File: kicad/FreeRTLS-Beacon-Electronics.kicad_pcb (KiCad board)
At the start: 2 copper layers, 52.5 x 33.5 mm, 0 parts

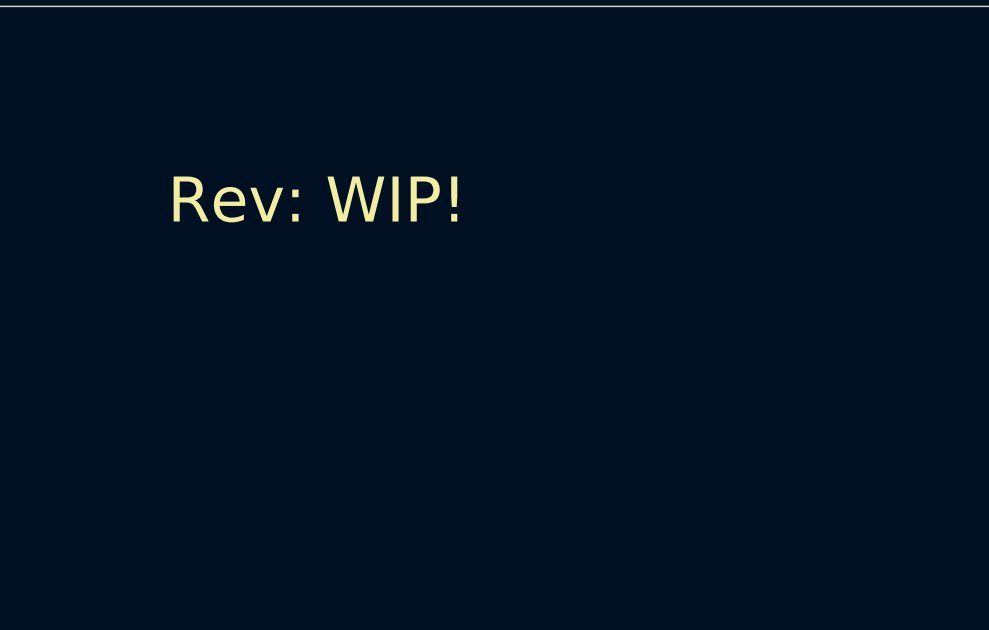
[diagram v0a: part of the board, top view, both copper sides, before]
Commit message: Add trace to test cnc file generation
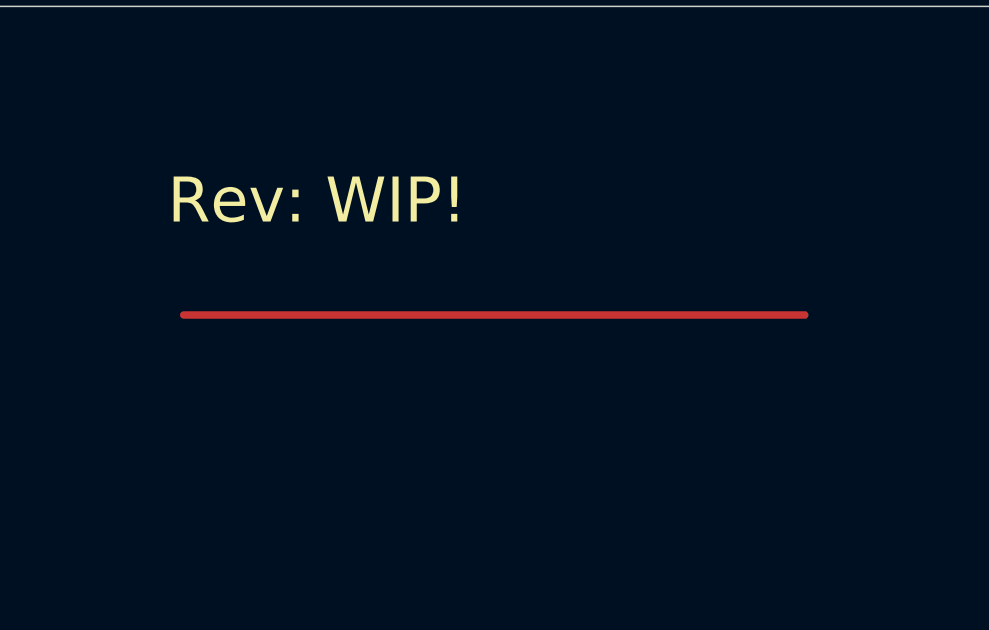
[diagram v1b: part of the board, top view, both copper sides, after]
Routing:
- net (no net): track 0.00 -> 20.7 mm
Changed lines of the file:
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@@
     (thickness 1.6)
     (drawings 5)
-    (tracks 0)
+    (tracks 1)
     (zones 0)
     (modules 0)
@@
     (effects (font (size 1.5 1.5) (thickness 0.3)))
   )
+  (segment (start 93.218 70.866) (end 113.919 70.866) (width 0.25) (layer F.Cu) (net 0))
 )

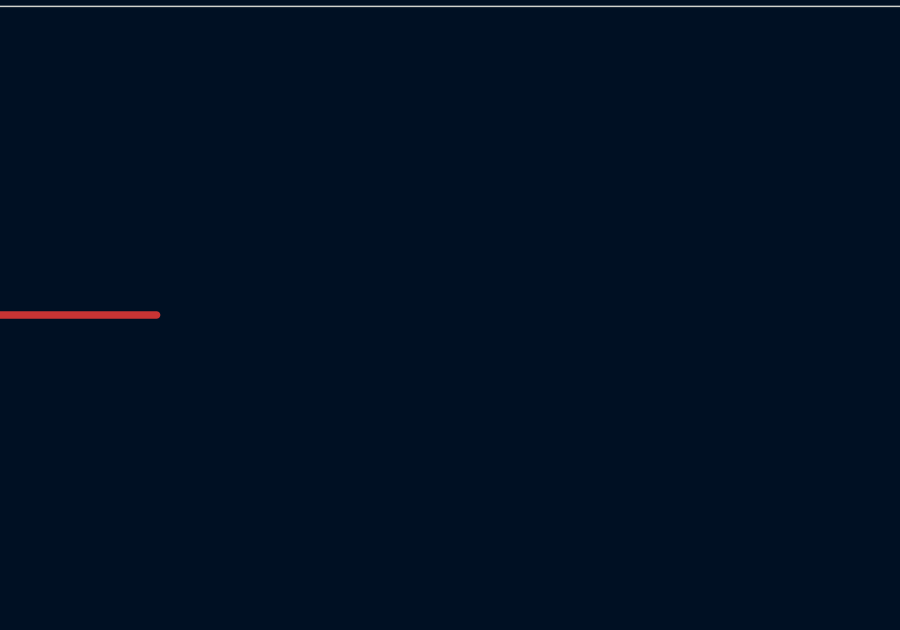
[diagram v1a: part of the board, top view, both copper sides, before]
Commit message: Add via to test cnc file generation
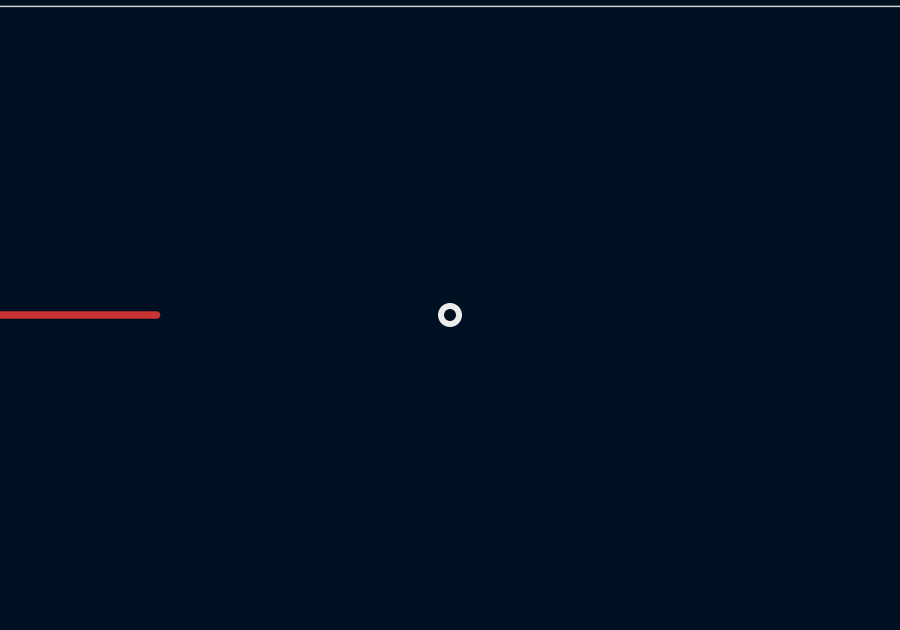
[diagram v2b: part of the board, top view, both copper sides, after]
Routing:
- net (no net): vias 0 -> 1
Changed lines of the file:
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@@
     (thickness 1.6)
     (drawings 5)
-    (tracks 1)
+    (tracks 2)
     (zones 0)
     (modules 0)
@@
   )
   (segment (start 93.218 70.866) (end 113.919 70.866) (width 0.25) (layer F.Cu) (net 0))
+  (via (at 123.698 70.866) (size 0.8) (drill 0.4) (layers F.Cu B.Cu) (net 0))
 )

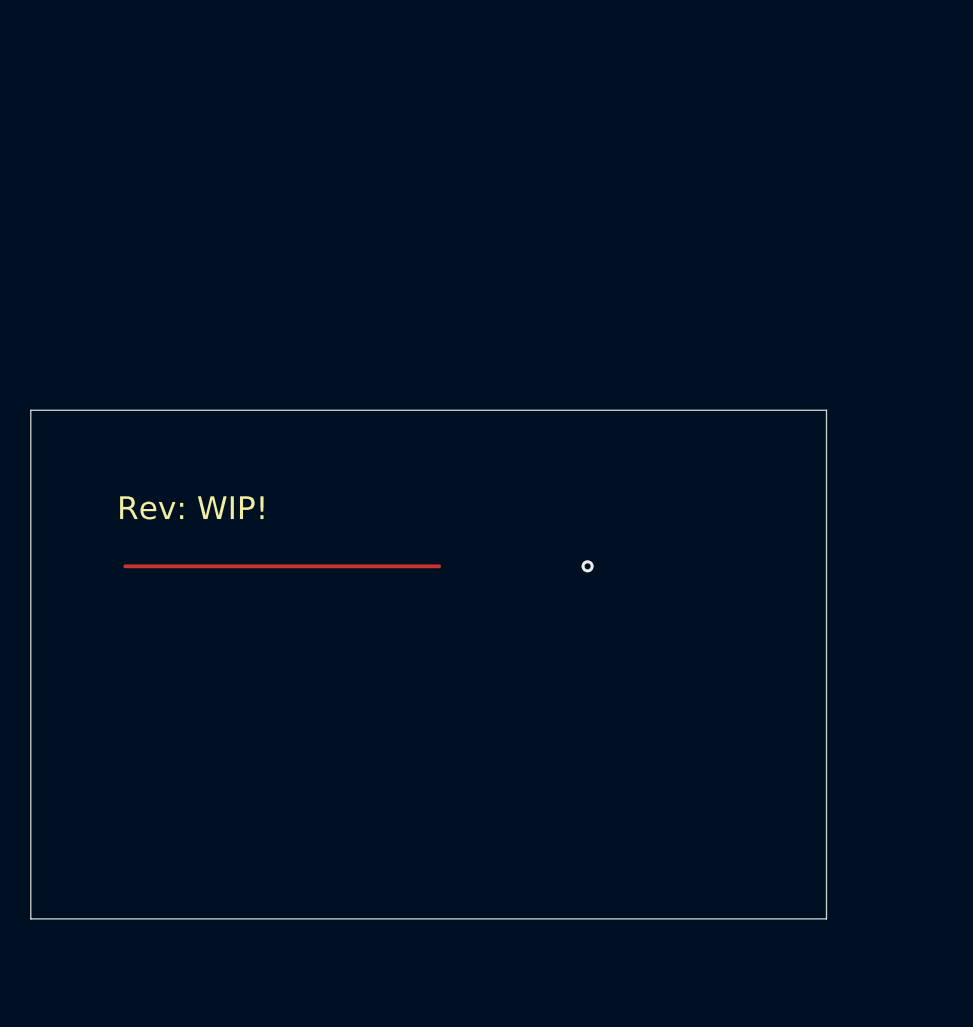
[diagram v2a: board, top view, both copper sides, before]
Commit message: Assign footprints
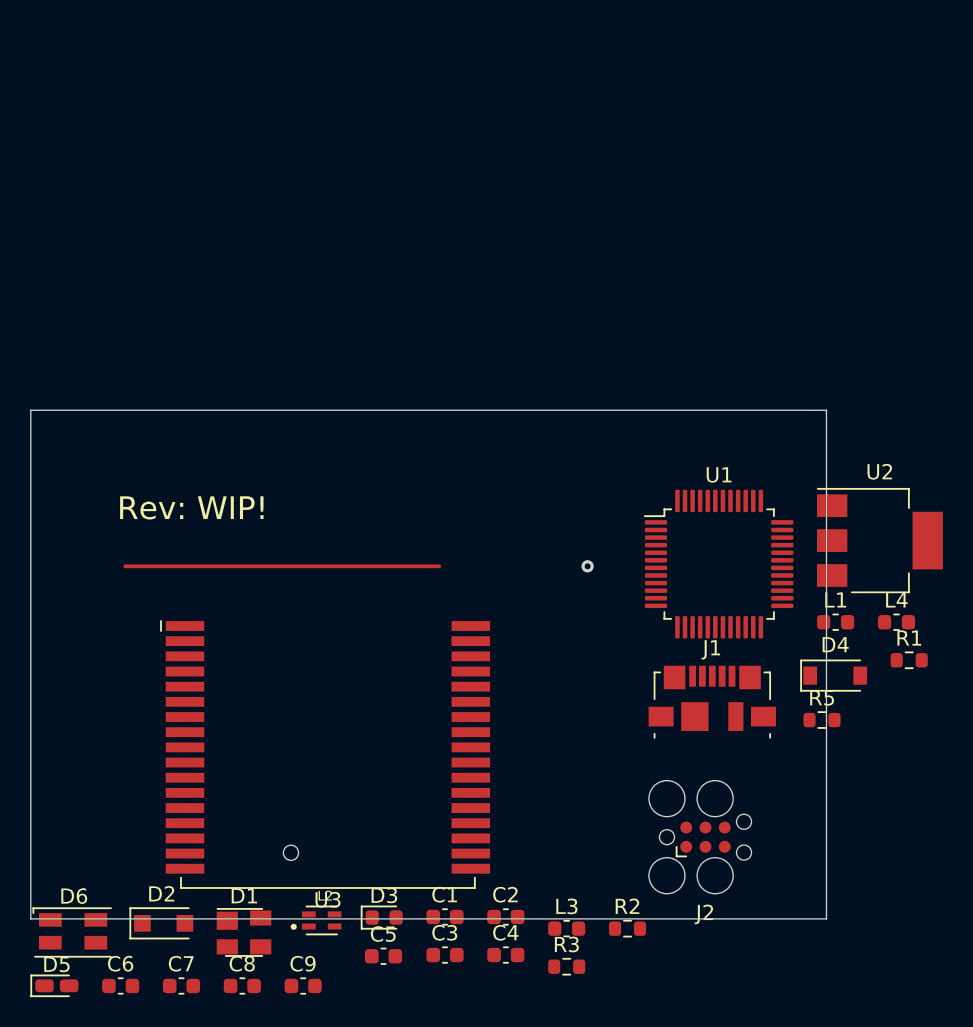
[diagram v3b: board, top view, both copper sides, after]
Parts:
- added C1: 1uF, Capacitor_SMD:C_0603_1608Metric, F.Cu at (114.3, 94.0)
- added C2: 100nF, Capacitor_SMD:C_0603_1608Metric, F.Cu at (118.3, 94.0)
- added C3: 100nF, Capacitor_SMD:C_0603_1608Metric, F.Cu at (114.3, 96.5)
- added C4: 100nF, Capacitor_SMD:C_0603_1608Metric, F.Cu at (118.3, 96.5)
- added C5: 100nF, Capacitor_SMD:C_0603_1608Metric, F.Cu at (110.2, 96.6)
- added C6: 10uF, Capacitor_SMD:C_0603_1608Metric, F.Cu at (92.9, 98.5)
- added C7: 10uF, Capacitor_SMD:C_0603_1608Metric, F.Cu at (96.9, 98.5)
- added C8: 10uF, Capacitor_SMD:C_0603_1608Metric, F.Cu at (100.9, 98.5)
- added C9: 100nF, Capacitor_SMD:C_0603_1608Metric, F.Cu at (105.0, 98.5)
- added D1: PRTR5V0U2X, Package_TO_SOT_SMD:SOT-143, F.Cu at (101.0, 95.0)
- added D2: PMEG3020EH, Diode_SMD:D_SOD-123F, F.Cu at (95.8, 94.4)
- added D3: LED GREEN, LED_SMD:LED_0603_1608Metric, F.Cu at (110.3, 94.0)
- added D4: 5.6V 1W, Diode_SMD:D_SOD-123, F.Cu at (140.0, 78.1)
- added D5: LED RED, LED_SMD:LED_0603_1608Metric_Castellated, F.Cu at (88.7, 98.5)
- added D6: L955QEQGC-TR, FreeRTLS-Beacon:LED_L955QEQGC-TR_3.2x2.7mm_P1.7mm, F.Cu at (89.8, 94.9)
- added J1: USB_B_Micro, Connector_USB:USB_Micro-B_Molex_47346-0001, F.Cu at (131.9, 79.6)
- added J2: TC2030, Connector:Tag-Connect_TC2030-IDC-FP_2x03_P1.27mm_Vertical, F.Cu at (131.5, 88.7)
- added L1: MPZ1608S221ATA00, Inductor_SMD:L_0603_1608Metric, F.Cu at (140.1, 74.5)
- added L2: DLW21HN900SQ2, FreeRTLS-Beacon:FIL_DLW21HN900SQ2L, F.Cu at (106.2, 94.2)
- added L3: MPZ1608S601ATA00, Inductor_SMD:L_0603_1608Metric, F.Cu at (122.3, 94.8)
- added L4: MPZ1608S221ATA00, Inductor_SMD:L_0603_1608Metric, F.Cu at (144.1, 74.5)
- added R1: 1k, Resistor_SMD:R_0603_1608Metric, F.Cu at (144.9, 77.1)
- added R2: 1k, Resistor_SMD:R_0603_1608Metric, F.Cu at (126.3, 94.8)
- added R3: 1k, Resistor_SMD:R_0603_1608Metric, F.Cu at (122.3, 97.3)
- added R5: 470, Resistor_SMD:R_0603_1608Metric, F.Cu at (139.2, 81.0)
- added U1: STM32F072CBTx, Package_QFP:LQFP-48_7x7mm_P0.5mm, F.Cu at (132.4, 70.7)
- added U2: AZ1117IH-3.3TRG1, Package_TO_SOT_SMD:SOT-223-3_TabPin2, F.Cu at (143.0, 69.2)
- added U3: DWM1001, RF_Module:DecaWave_DWM1001, F.Cu at (106.6, 82.9)

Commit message: Place all components and route some
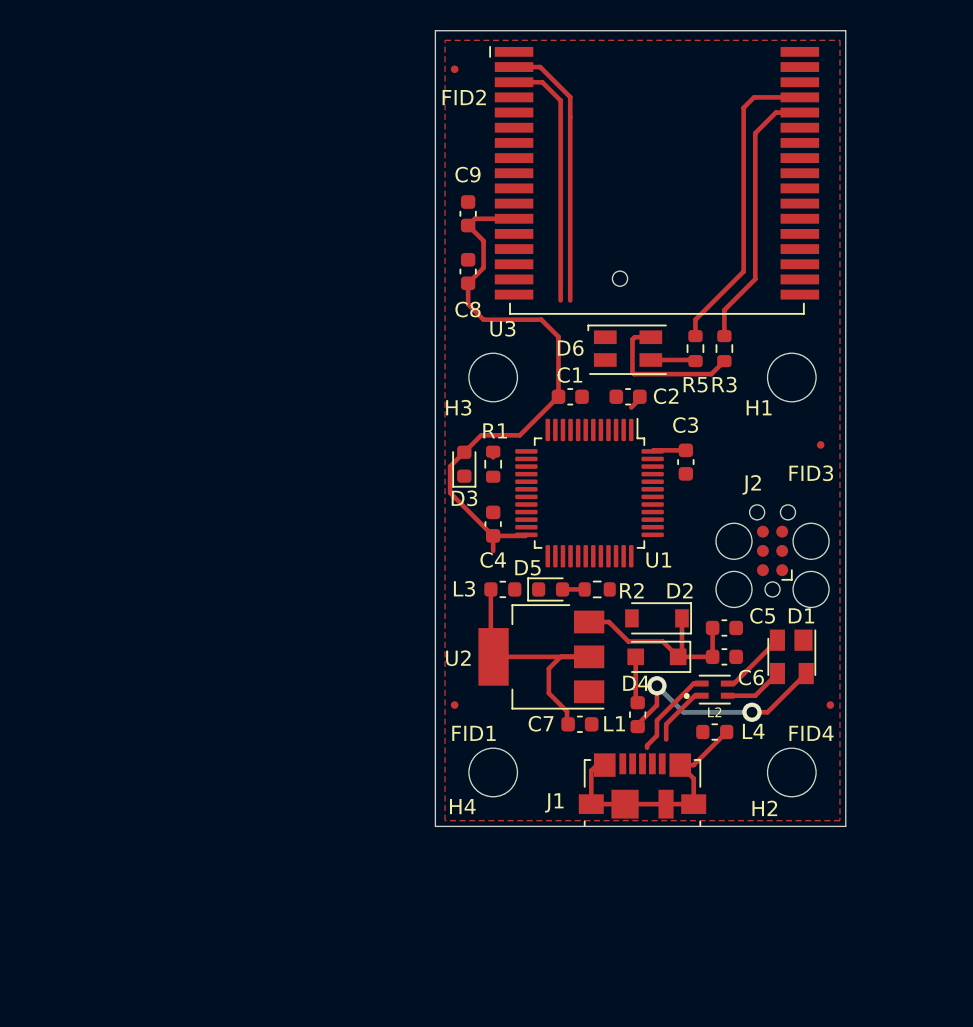
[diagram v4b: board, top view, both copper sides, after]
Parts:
- added FID1: Fiducial, Fiducial:Fiducial_0.5mm_Mask1.5mm, F.Cu at (114.9, 80.0)
- added FID2: Fiducial, Fiducial:Fiducial_0.5mm_Mask1.5mm, F.Cu at (114.9, 38.1)
- added FID3: Fiducial, Fiducial:Fiducial_0.5mm_Mask1.5mm, F.Cu at (139.1, 62.9)
- added FID4: Fiducial, Fiducial:Fiducial_0.5mm_Mask1.5mm, F.Cu at (139.7, 80.0)
- added H1: MountingHole, MountingHole:MountingHole_3.2mm_M3, F.Cu at (137.2, 58.4)
- added H2: MountingHole, MountingHole:MountingHole_3.2mm_M3, F.Cu at (137.2, 84.5)
- added H3: MountingHole, MountingHole:MountingHole_3.2mm_M3, F.Cu at (117.5, 58.4)
- added H4: MountingHole, MountingHole:MountingHole_3.2mm_M3, F.Cu at (117.5, 84.5)
- added REF**: OSHW-Logo_5.7x6mm_SilkScreen, Symbol:OSHW-Logo_5.7x6mm_SilkScreen, B.Cu at (127.3, 70.2)
- D3: value LED GREEN -> J-Link Status
- D5: value LED RED -> Power On; footprint LED_SMD:LED_0603_1608Metric_Castellated -> LED_SMD:LED_0603_1608Metric
- D6: value L955QEQGC-TR -> DW1000 Tx / Rx
- J2: value TC2030 -> STM Prog
- moved D6 53.0 mm to (126.4, 56.5)
- moved C9 52.1 mm to (115.8, 47.6), turned to 90 degrees
- moved C8 49.4 mm to (115.8, 51.4), turned to 90 degrees
- moved C6 45.3 mm to (132.7, 76.8)
- moved U3 43.6 mm to (128.3, 45.1)
- moved R3 42.1 mm to (132.7, 56.5), turned to 90 degrees
- moved D5 41.7 mm to (121.3, 72.4)
- moved D1 40.4 mm to (137.2, 76.8), turned to 270 degrees
- moved D2 37.0 mm to (128.3, 76.8), turned to 180 degrees
- moved C3 36.2 mm to (130.2, 64.0), turned to 270 degrees
- moved C1 35.3 mm to (122.6, 59.7)
- moved C2 35.2 mm to (126.4, 59.7), turned to 180 degrees
- moved C7 31.4 mm to (123.2, 81.3)
- moved C5 31.2 mm to (132.7, 74.9)
- moved D3 30.3 mm to (115.6, 64.1), turned to 90 degrees
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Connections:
- R2 pad 1: Net-(C5-Pad1) -> +3V3
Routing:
- net +3V3: track 0.00 -> 41.2 mm
- net (no net): track 20.7 -> 0.00 mm, vias 1 -> 0
- net Net-(R5-Pad2): track 0.00 -> 20.4 mm
- net Net-(C7-Pad1): track 0.00 -> 18.0 mm
- net /SWCLK: track 0.00 -> 17.9 mm
- net Net-(R3-Pad2): track 0.00 -> 17.7 mm
- net Net-(J1-Pad6): track 0.00 -> 16.9 mm
- net /SWDIO: track 0.00 -> 16.7 mm
- net VBUS: track 0.00 -> 14.8 mm, vias 0 -> 2
- net Net-(C5-Pad1): track 0.00 -> 14.3 mm
- net Net-(D6-Pad2): track 0.00 -> 9.89 mm
- net Net-(J1-Pad2): track 0.00 -> 6.04 mm
- net /MCU_D-: track 0.00 -> 4.46 mm
- net Net-(J1-Pad3): track 0.00 -> 4.13 mm
- net /MCU_D+: track 0.00 -> 3.88 mm
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- added copper zone on F.Cu, net GND
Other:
- board size 52.5 x 33.5 mm -> 27.1 x 52.5 mm
- net class Default: clearance 0.2 -> 0.3048; trace_width 0.25 -> 0.3048; via_dia 0.8 -> 1.27; via_drill 0.4 -> 0.7112
- rule trace_clearance: 0.2 -> 0.3048
- rule trace_min: 0.2 -> 0.3048
- rule via_min_drill: 0.3 -> 0.7112
- rule via_min_size: 0.4 -> 1.27
- board text added: "FreeRTLS Beacon Electronics"

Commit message: Finish routing
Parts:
- removed REF**: OSHW-Logo_5.7x6mm_SilkScreen, Symbol:OSHW-Logo_5.7x6mm_SilkScreen
- moved J2 2.32 mm to (135.5, 67.6)
- moved D5 2.03 mm to (119.2, 72.4)
- moved L3 2.03 mm to (116.1, 72.4)
- moved R2 2.03 mm to (122.3, 72.4)
- moved FID3 0.25 mm to (139.1, 62.6)
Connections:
- D1 pad 2: /MCU_D- -> /MCU_D+
- D1 pad 3: /MCU_D+ -> /MCU_D-
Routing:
- net +3V3: track 41.2 -> 98.7 mm, vias 0 -> 2
- net /STM_RESET: track 0.00 -> 30.1 mm, vias 0 -> 2
- net /TXD: track 0.00 -> 29.4 mm, vias 0 -> 2
- net /RXD: track 0.00 -> 27.9 mm, vias 0 -> 2
- net /MCU_D+: track 3.88 -> 22.7 mm
- net /SWDIO: track 16.7 -> 32.4 mm
- net /MCU_D-: track 4.46 -> 19.7 mm
- net Net-(J2-Pad2): track 0.00 -> 14.1 mm
- net /SWCLK: track 17.9 -> 27.3 mm
- net Net-(J2-Pad4): track 0.00 -> 7.39 mm
- net Net-(R1-Pad1): track 0.05 -> 5.82 mm
- net VBUS: track 14.8 -> 17.5 mm
- net Net-(J1-Pad3): track 4.13 -> 6.52 mm
- net Net-(D3-Pad1): track 0.00 -> 1.92 mm
- net Net-(J1-Pad2): track 6.04 -> 7.67 mm
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- added copper zone on B.Cu, net GND
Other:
- net class 10 added: clearance 0.254, trace_width 0.3048, via_dia 1.27, via_drill 0.7112
- net class 8/8 added: clearance 0.1778, trace_width 0.1778, via_dia 1.27, via_drill 0.7112
- net class Clear 7 added: clearance 0.1778, trace_width 0.3048, via_dia 1.27, via_drill 0.7112
- net class GND added: clearance 0.1778, trace_width 0.1778, via_dia 1.27, via_drill 0.7112
- rule trace_min: 0.3048 -> 0.1524

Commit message: Add PCBWay PCB Specification
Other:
- board text added: "PCBWay PCB Specification —————————————————— - Board type: Single pieces - Different Design in Panel: 1 - Size (single): 27.05 mm x 52.45 mm - Layers: 2 Layers - Material: FR-4 - FR4-TG: TG 130-140 - Thickness: 1.6 - Min Track/Spacing: 8/8 mil - Min Hole Size: 0.3 mm - Solder Mask: Purple (Prototype) - Black (Pre-Release) - Green (Release) - Silkscreen: White - Gold fingers: No - Surface Finish: H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"

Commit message: Add OSH logo
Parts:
- added REF**: OSHW-Logo2_7.3x6mm_SilkScreen, Symbol:OSHW-Logo2_7.3x6mm_SilkScreen, B.Cu at (119.5, 50.4)

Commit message: Add OSH logo
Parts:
- removed REF**: OSHW-Logo2_7.3x6mm_SilkScreen, Symbol:OSHW-Logo2_7.3x6mm_SilkScreen
- added LOGO1: Logo_Open_Hardware_Small, Symbol:OSHW-Logo_5.7x6mm_SilkScreen, B.Cu at (119.3, 49.8)
